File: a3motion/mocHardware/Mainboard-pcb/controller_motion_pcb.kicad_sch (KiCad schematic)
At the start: 42 parts, among them J1 SPI_Female, J2 SPI_Male, J3 Conn_01x06_Female, J4 UPDI_Interface, J5 Programm_Jumper, SW1 Rotary_Encoder_Switch, U1 TPIC6C595-SOIC, U2 TPIC6C595-SOIC, U3 ATtiny1626

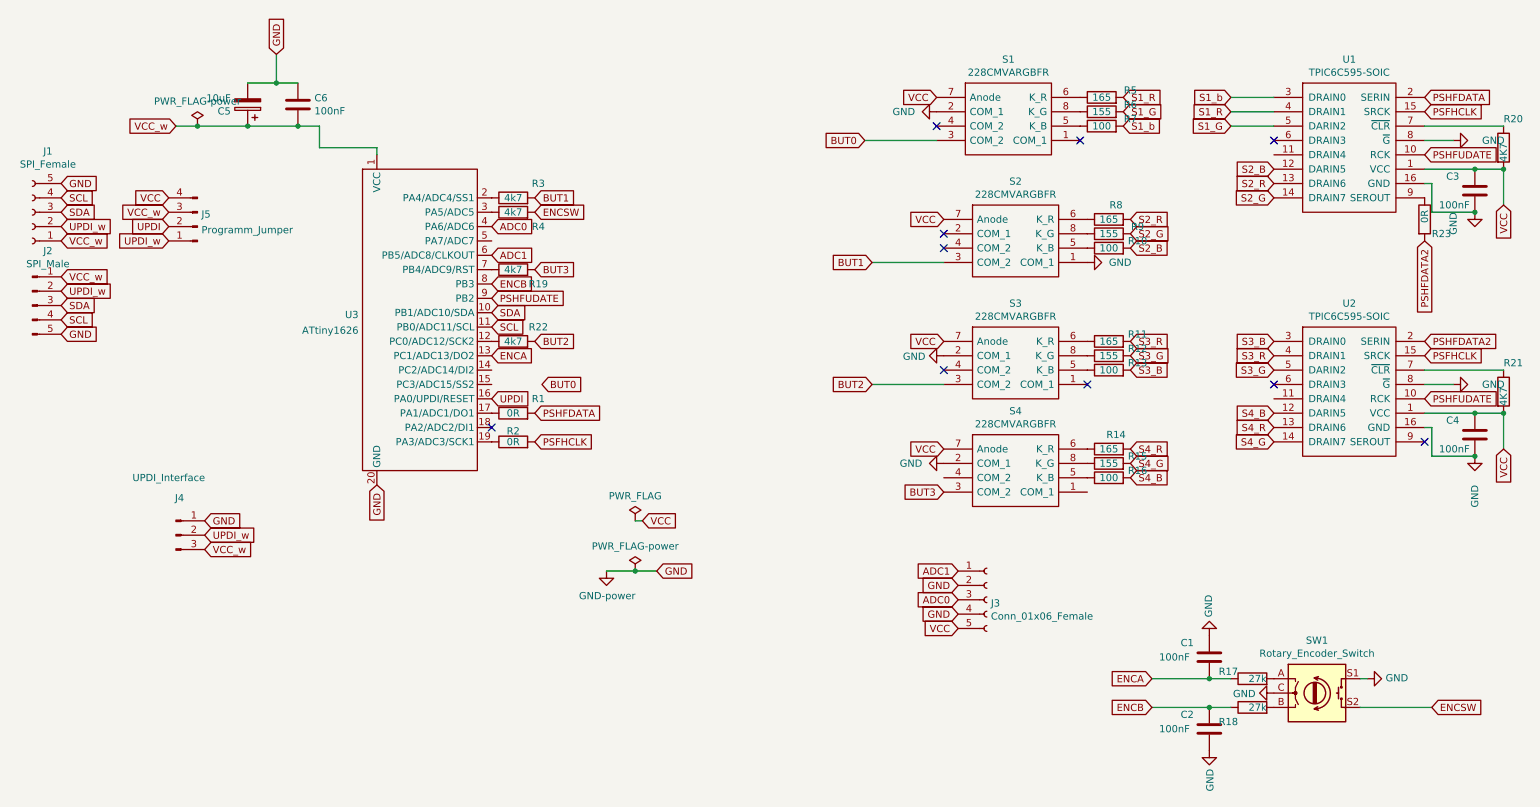
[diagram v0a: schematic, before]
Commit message: cleaned libs and finished main und rpi pcb
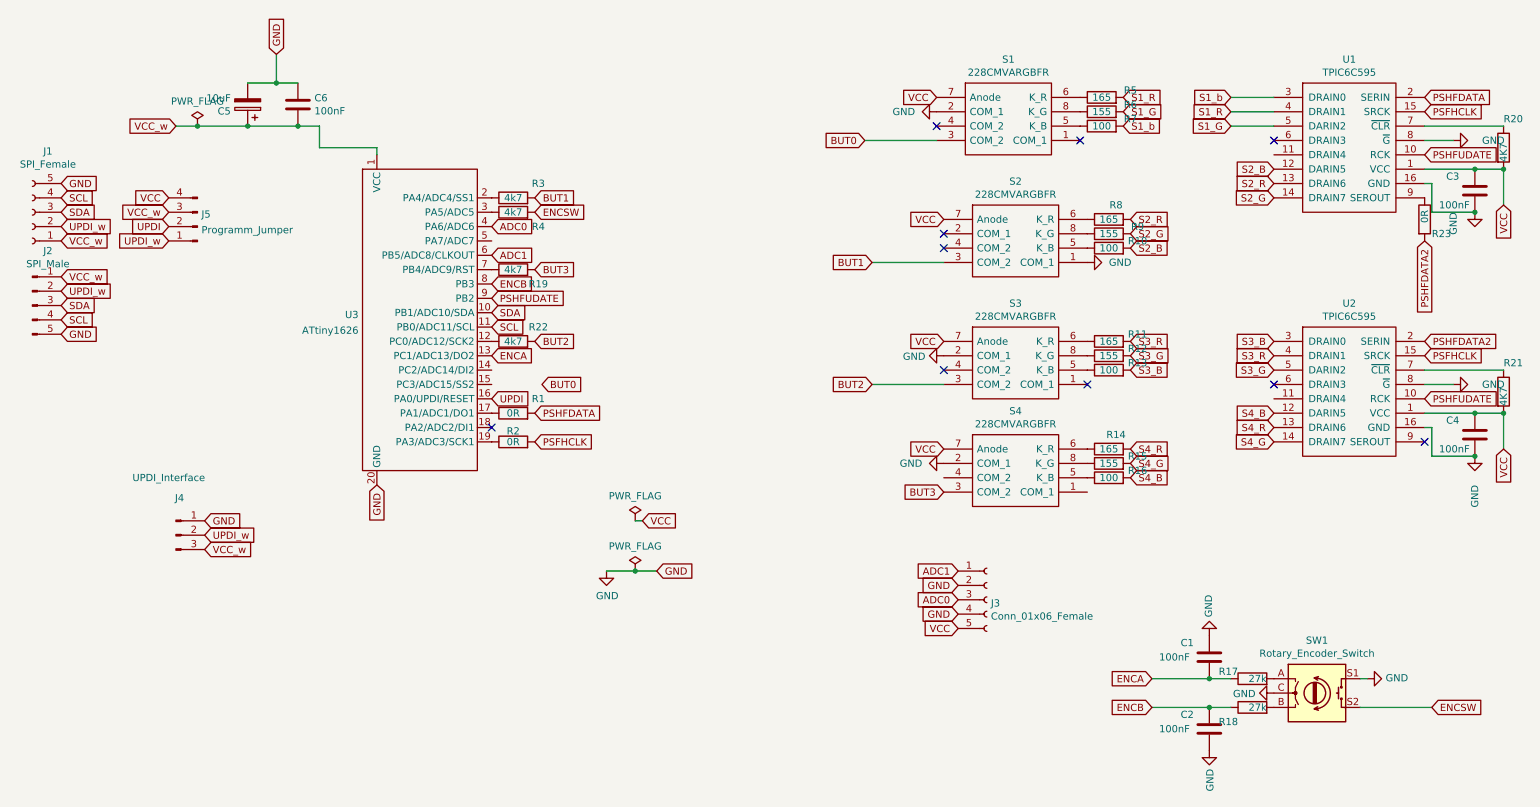
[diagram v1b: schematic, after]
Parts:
- S1, S2, S3, S4: footprint MOUSERfootprintANDsymbol:228CMVARGBFR -> 3dAudioFoot:228CMVARGBFR_SMD; symbol btn-matrix-rescue:228CMVARGBFR -> 3dAudioSym:228CMVARGBFR
- SW1: footprint MOUSERfootprintANDsymbol:PEC11R4230KS0024 -> 3dAudioFoot:PEC11R4230KS0024
- U1, U2: value TPIC6C595-SOIC -> TPIC6C595; symbol flex_AmbisonicLib:TPIC6C595-SOIC -> 3dAudioSym:TPIC6C595
- U3: footprint .Ambisonic:attiny1626 -> 3dAudioFoot:attiny1626; symbol .Ambisonic:ATtiny1626 -> 3dAudioSym:ATtiny1626
